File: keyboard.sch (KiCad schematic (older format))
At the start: 84 parts, among them IC1 ATMEGA32U4, J1 MINI, P1 CONN_1, P10 CONN_1, P11 CONN_1, P12 CONN_1, P13 CONN_1, P14 CONN_1, P15 CONN_1, P16 CONN_1, P17 CONN_1, P18 CONN_1, P19 CONN_1, P2 CONN_1, P20 CONN_1, P21 CONN_1, P22 CONN_1, P23 CONN_1, P24 CONN_1, P25 CONN_1, P26 CONN_1, P27 CONN_1, P28 CONN_1, P29 CONN_1, P3 CONN_1, P30 CONN_1, P31 CONN_1, P32 CONN_1, P33 CONN_1, P34 CONN_1, P35 CONN_1, P36 CONN_1, P37 CONN_1, P38 CONN_1, P39 CONN_1, P4 CONN_1, P40 CONN_1, P41 CONN_1, P42 CONN_1, P5 CONN_1, P6 CONN_1, P7 CONN_1, P8 CONN_1, P9 CONN_1, X1 ASX3F

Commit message: Remap symbols
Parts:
- C1, C2, C3, C4, C5, C6, C7, C8: symbol C -> keyboard-rescue:C-device
- DF10, DF11, DF20, DF201, DF21, DF211, DF22, DF221, DF23, DF231, DF232, DF3, DW1, DW2, DW3, DW4: symbol LED -> keyboard-rescue:LED-device
- IC1: symbol ATMEGA32U4 -> keyboard-rescue:ATMEGA32U4-atmega32u4
- J1: symbol USBMINI_B05 -> keyboard-rescue:USBMINI_B05-oupiin_usb
- P1, P10, P11, P12, P13, P14, P15, P16, P17, P18, P19, P2, P20, P21, P22, P23, P24, P25, P26, P27, P28, P29, P3, P30, P31, P32, P33, P34, P35, P36, P37, P38, P39, P4, P40, P41, P42, P5, P6, P7, P8, P9: symbol CONN_1 -> keyboard-rescue:CONN_1-conn
- R1, R10, R11, R12, R13, R14, R15, R2, R3, R5, R6, R7, R8, R9: symbol R -> keyboard-rescue:R-device
- S0: symbol DTSM-6 -> keyboard-rescue:DTSM-6-dtsjw
- X1: symbol ASX4 -> keyboard-rescue:ASX4-aker
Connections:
- wire segments 205 -> 245

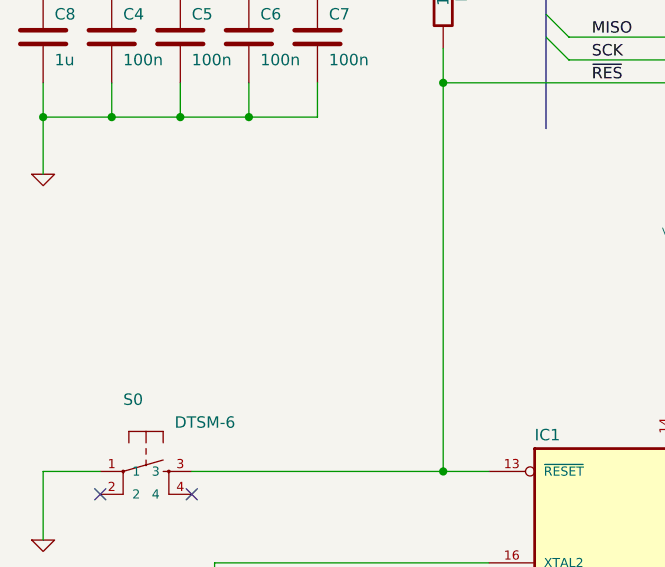
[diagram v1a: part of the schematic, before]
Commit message: Add nRF52840 MCU sheet
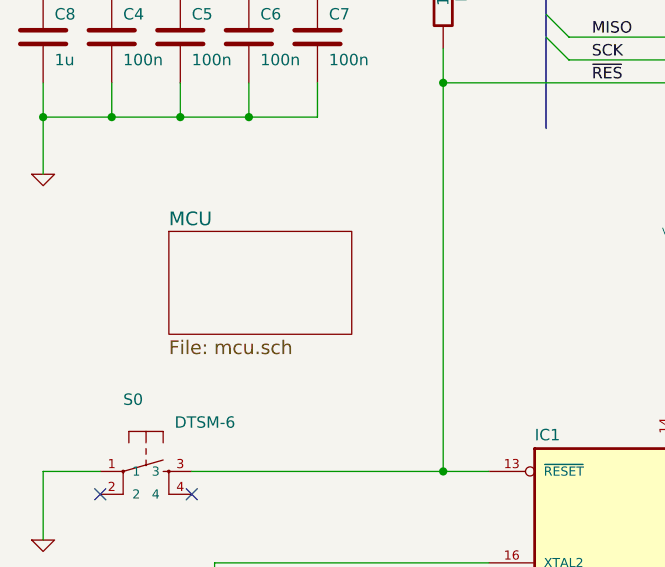
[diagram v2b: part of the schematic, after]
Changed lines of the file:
@@
 $Descr A4 11693 8268
 encoding utf-8
-Sheet 1 3
+Sheet 1 4
 Title "ukbdc - schematic"
 Date "17 jul 2013"
@@
 Wire Wire Line
 	800  1650 800  1900
+$Sheet
+S 1350 2150 800  450
+U 5CFC508C
+F0 "MCU" 60
+F1 "mcu.sch" 60
+$EndSheet
 Wire Bus Line
 	3000 900  3000 1700
